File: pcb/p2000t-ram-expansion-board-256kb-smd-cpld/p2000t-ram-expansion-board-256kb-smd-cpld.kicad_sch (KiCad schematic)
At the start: 15 parts, among them J1 EXPANSION BOARD, J2 POWER, J3 TERMINAL, J4 Atmel-JTAG-10, U1 ATF1502ASV, U2 62128, U3 62128

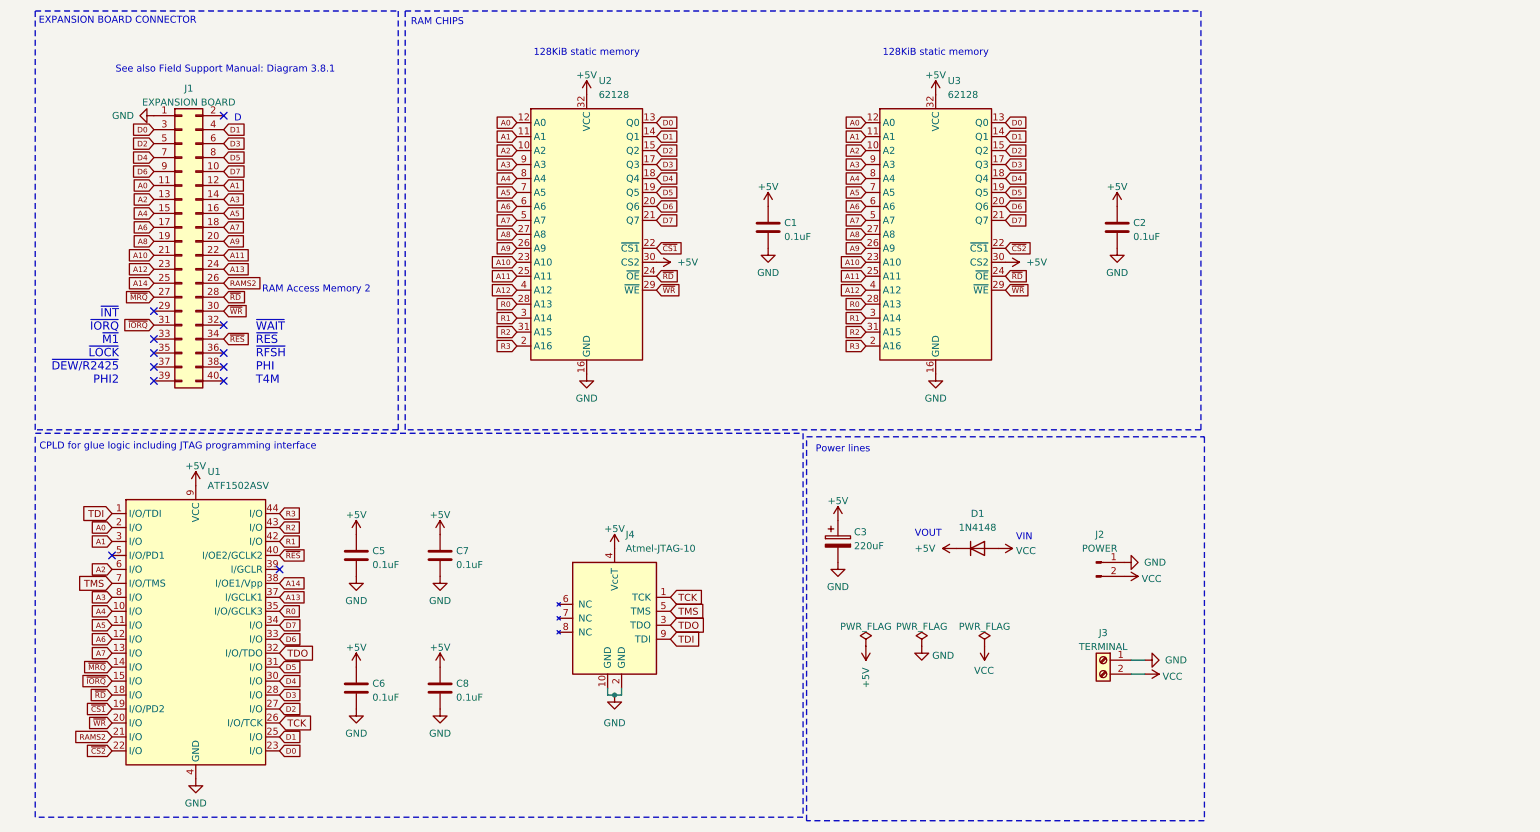
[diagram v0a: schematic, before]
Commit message: Expanding to 4 RAM chips
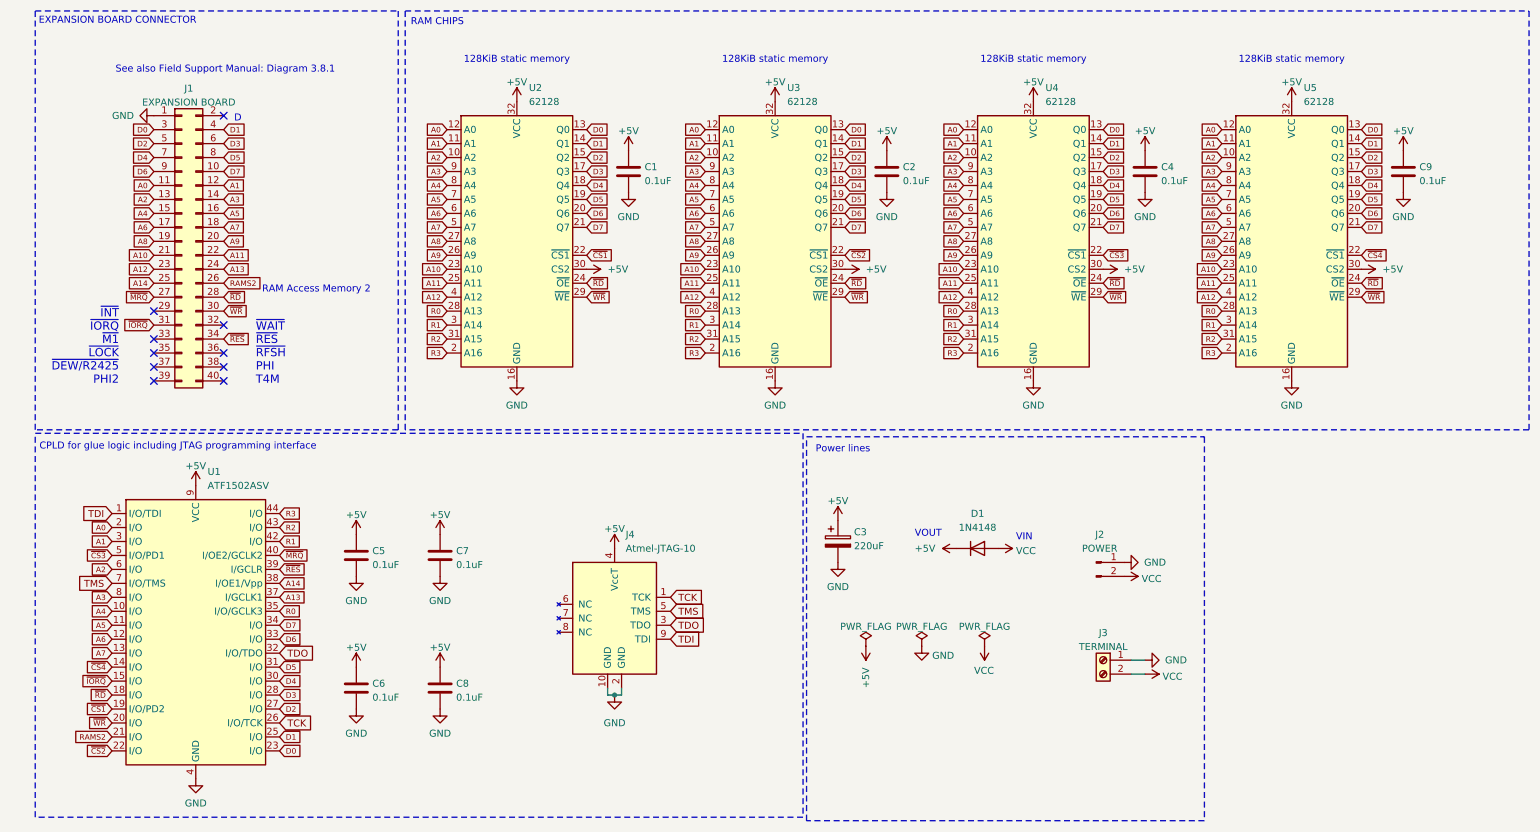
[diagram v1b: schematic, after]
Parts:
- added C4, C9: 0.1uF, Capacitor_SMD:C_0805_2012Metric_Pad1.18x1.45mm_HandSolder, symbol Device:C
- added U4, U5: 62128, Package_SO:TSOP-I-32_18.4x8mm_P0.5mm, symbol Memory_RAM:628128_DIP32_SSOP32
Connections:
- net +5V: now also C4.1, C9.1, U4.30 (CS2), U4.32 (VCC), U5.30 (CS2), U5.32 (VCC)
- net A0: now also U4.12 (A0), U5.12 (A0)
- net A1: now also U4.11 (A1), U5.11 (A1)
- net A10: now also U4.23 (A10), U5.23 (A10)
- net A11: now also U4.25 (A11), U5.25 (A11)
- net A12: now also U4.4 (A12), U5.4 (A12)
- net A2: now also U4.10 (A2), U5.10 (A2)
- net A3: now also U4.9 (A3), U5.9 (A3)
- net A4: now also U4.8 (A4), U5.8 (A4)
- net A5: now also U4.7 (A5), U5.7 (A5)
- net A6: now also U4.6 (A6), U5.6 (A6)
- net A7: now also U4.5 (A7), U5.5 (A7)
- net A8: now also U4.27 (A8), U5.27 (A8)
- net A9: now also U4.26 (A9), U5.26 (A9)
- net D0: now also U4.13 (Q0), U5.13 (Q0)
- net D1: now also U4.14 (Q1), U5.14 (Q1)
- net D2: now also U4.15 (Q2), U5.15 (Q2)
- net D3: now also U4.17 (Q3), U5.17 (Q3)
- net D4: now also U4.18 (Q4), U5.18 (Q4)
- net D5: now also U4.19 (Q5), U5.19 (Q5)
- net D6: now also U4.20 (Q6), U5.20 (Q6)
- net D7: now also U4.21 (Q7), U5.21 (Q7)
- net GND: now also C4.2, C9.2, U4.16 (GND), U5.16 (GND)
- net R0: now also U4.28 (A13), U5.28 (A13)
- net R1: now also U4.3 (A14), U5.3 (A14)
- net R2: now also U4.31 (A15), U5.31 (A15)
- net R3: now also U4.2 (A16), U5.2 (A16)
- net ~{MRQ}: now also U1.40 (I/OE2/GCLK2); no longer U1.14 (I/O)
- net ~{RD}: now also U4.24 (~{OE}), U5.24 (~{OE})
- net ~{RES}: now also U1.39 (I/GCLR); no longer U1.40 (I/OE2/GCLK2)
- net ~{WR}: now also U4.29 (~{WE}), U5.29 (~{WE})
- net ~{CS3}: now reaches U1.5 (I/O/PD1)
- net ~{CS3}: now also U4.22 (~{CS1})
- new net ~{CS4}: U1.14 (I/O), U5.22 (~{CS1})
- no-connect marks 12 -> 10
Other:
- moved on the sheet: C1, C2, U2, U3
